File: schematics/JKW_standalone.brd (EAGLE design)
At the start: 159.4 x 80.7 mm, 225 parts, among them IC1 4093D, IC4 ATMEGA2560-16AU, Q1 BSS84, Q10 BSS84, Q11 BSS84, Q2 BSS84, Q3 BSS84, Q4 BSS84, Q5 BSS84, Q6 BSS84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

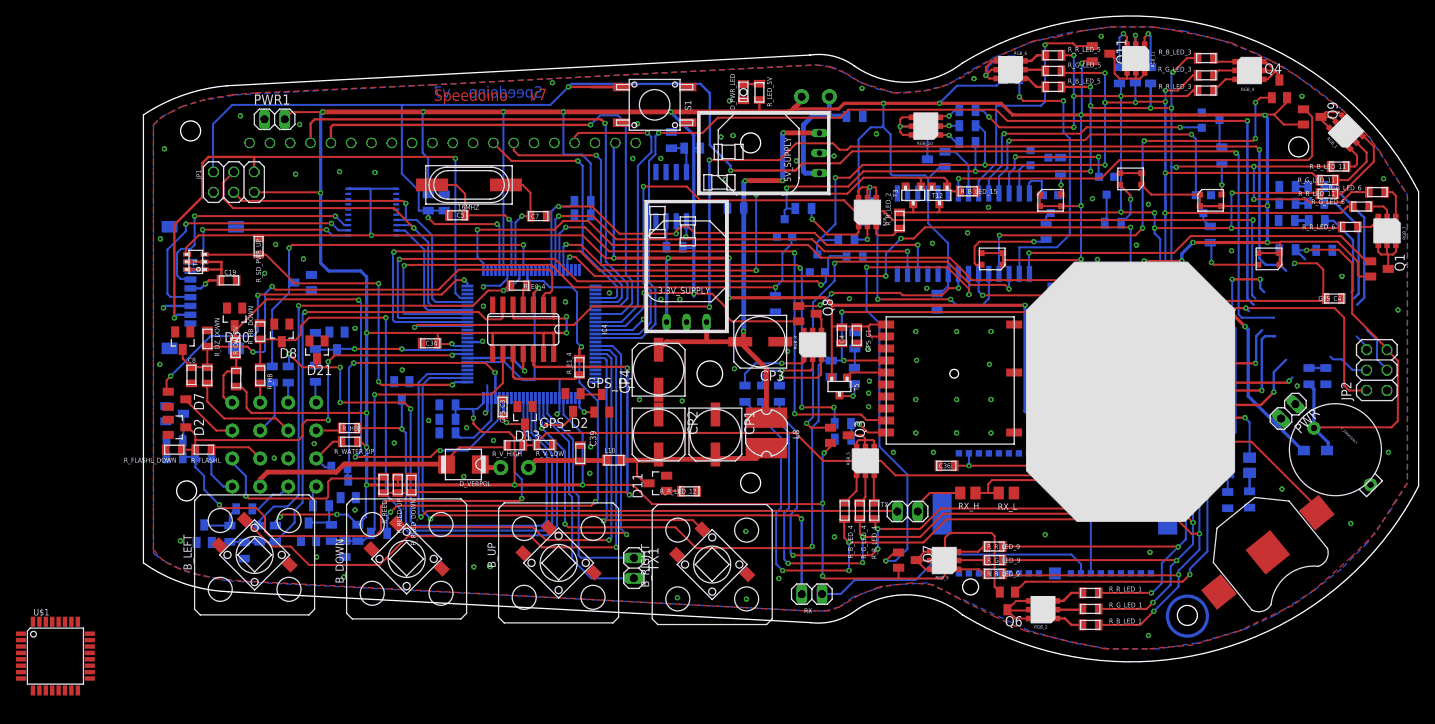
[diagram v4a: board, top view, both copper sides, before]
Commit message: Moved AT in place
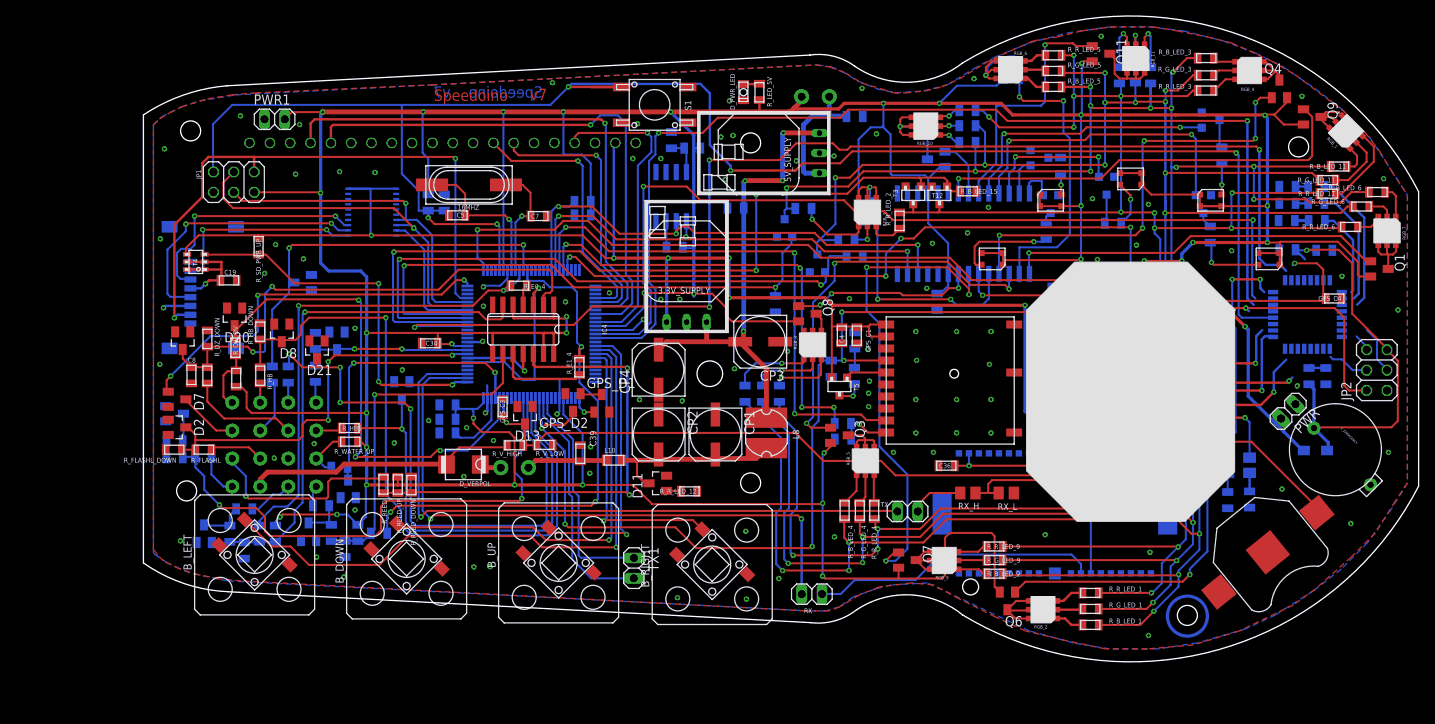
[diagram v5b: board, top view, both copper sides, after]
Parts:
- moved U$1 162.2 mm to (145.5, 38.8), flipped to the bottom, turned to 270 degrees
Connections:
- net RESETAVR_AT8: now also U$1.29
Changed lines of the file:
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@@
 <?xml version="1.0" encoding="utf-8"?>
 <!DOCTYPE eagle SYSTEM "eagle.dtd">
-<eagle version="6.2">
+<eagle version="6.1">
 <drawing>
 <settings>
@@
 <element name="U$22" library="Kolja" package="PLCC-4" value="CLM4B-RKW-CWAXBAA3" x="123.4" y="35.6" rot="R180"/>
 <element name="R_L3" library="RCLDT" package="0805" value="1k" x="125" y="43.1" rot="MR270"/>
-<element name="U$1" library="Kolja" package="TQFP8" value="ATMEGA328P-AU" x="-11" y="-3.9"/>
+<element name="U$1" library="Kolja" package="TQFP8" value="ATMEGA328P-AU" x="145.5" y="38.8" rot="MR270"/>
 </elements>
 <signals>
@@
 <wire x1="37.3017375" y1="7.03024375" x2="41.3" y2="7.25" width="0" layer="19" extent="1-1"/>
 <wire x1="119.725" y1="73.575" x2="132.2887" y2="64.0524" width="0" layer="19" extent="16-16"/>
-<wire x1="-6.7074" y1="-3.5" x2="4.625" y2="10.5" width="0" layer="19" extent="1-1"/>
-<wire x1="-15.2926" y1="-4.3" x2="-6.7074" y2="-3.5" width="0" layer="19" extent="1-1"/>
-<wire x1="-15.2926" y1="-2.7" x2="-15.2926" y2="-4.3" width="0" layer="19" extent="1-1"/>
+<wire x1="145.1" y1="34.5074" x2="4.625" y2="10.5" width="0" layer="19" extent="1-1"/>
+<wire x1="145.9" y1="43.0926" x2="145.1" y2="34.5074" width="0" layer="19" extent="1-1"/>
+<wire x1="144.3" y1="43.0926" x2="145.9" y2="43.0926" width="0" layer="19" extent="1-1"/>
 </signal>
 <signal name="DZ">
@@
 <wire x1="136.1" y1="37.5" x2="136.5" y2="37.1" width="0.254" layer="16"/>
 <contactref element="U$1" pad="32"/>
-<wire x1="-13.8" y1="0.3926" x2="118.435" y2="21.44" width="0" layer="19" extent="1-16"/>
+<wire x1="141.2074" y1="41.6" x2="118.435" y2="21.44" width="0" layer="19" extent="1-16"/>
 </signal>
 <signal name="N$9">
@@
 <wire x1="139.1" y1="59.8" x2="139.5" y2="59.4" width="0.254" layer="1"/>
 <contactref element="U$1" pad="1"/>
-<wire x1="-15.2926" y1="-1.1" x2="33.9" y2="37.2" width="0" layer="19" extent="1-16"/>
+<wire x1="142.7" y1="43.0926" x2="33.9" y2="37.2" width="0" layer="19" extent="1-16"/>
 </signal>
 <signal name="D51">
@@
 <wire x1="136.4" y1="59.2" x2="136.6" y2="59" width="0.254" layer="1"/>
 <contactref element="U$1" pad="28"/>
-<wire x1="-10.6" y1="0.3926" x2="8.76" y2="56.62" width="0" layer="19" extent="1-1"/>
+<wire x1="141.2074" y1="38.4" x2="8.76" y2="56.62" width="0" layer="19" extent="1-1"/>
 </signal>
 <signal name="N$35">
@@
 <wire x1="64" y1="58.8" x2="64" y2="61.1" width="0.254" layer="16"/>
 <contactref element="U$1" pad="30"/>
-<wire x1="-12.2" y1="0.3926" x2="56.5" y2="35.86" width="0" layer="19" extent="1-16"/>
+<wire x1="141.2074" y1="40" x2="56.5" y2="35.86" width="0" layer="19" extent="1-16"/>
 </signal>
 <signal name="RX3">
@@
 <wire x1="62.5" y1="42.7" x2="62.5" y2="54.8" width="0.254" layer="16"/>
 <contactref element="U$1" pad="31"/>
-<wire x1="-13" y1="0.3926" x2="56.5" y2="36.36" width="0" layer="19" extent="1-16"/>
+<wire x1="141.2074" y1="40.8" x2="56.5" y2="36.36" width="0" layer="19" extent="1-16"/>
 </signal>
 <signal name="NG_IN">
@@
 <wire x1="81.5" y1="24" x2="50.4" y2="24" width="0.254" layer="1"/>
 <contactref element="U$1" pad="2"/>
-<wire x1="-15.2926" y1="-1.9" x2="44.9" y2="25.8" width="0" layer="19" extent="1-1"/>
+<wire x1="143.5" y1="43.0926" x2="44.9" y2="25.8" width="0" layer="19" extent="1-1"/>
 </signal>
 <signal name="A5">
@@
 <contactref element="U$1" pad="18"/>
 <contactref element="U$1" pad="20"/>
-<wire x1="-6.7074" y1="-4.3" x2="145.7" y2="32.116" width="0" layer="19" extent="1-16"/>
-<wire x1="-6.7074" y1="-5.9" x2="-6.7074" y2="-4.3" width="0" layer="19" extent="1-1"/>
+<wire x1="145.9" y1="34.5074" x2="145.7" y2="32.116" width="0" layer="19" extent="1-16"/>
+<wire x1="147.5" y1="34.5074" x2="145.9" y2="34.5074" width="0" layer="19" extent="1-1"/>
 </signal>
 <signal name="SCK_AT8">
@@
 <wire x1="149.8" y1="33.2" x2="151.15" y2="31.85" width="0.254" layer="16"/>
 <contactref element="U$1" pad="17"/>
-<wire x1="-6.7074" y1="-6.7" x2="148.3559" y2="33.5441" width="0" layer="19" extent="1-16"/>
+<wire x1="148.3" y1="34.5074" x2="148.3559" y2="33.5441" width="0" layer="19" extent="1-16"/>
 </signal>
 <signal name="MISO_AT8">
@@
 <wire x1="152.905" y1="34.795" x2="151.6259" y2="36.0741" width="0.254" layer="16"/>
 <contactref element="U$1" pad="16"/>
-<wire x1="-8.2" y1="-8.1926" x2="151.6259" y2="36.0741" width="0" layer="19" extent="1-16"/>
+<wire x1="149.7926" y1="36" x2="151.6259" y2="36.0741" width="0" layer="19" extent="1-16"/>
 </signal>
 <signal name="MOSI_AT8">
@@
 <wire x1="155.445" y1="31.85" x2="155.445" y2="31.955" width="0.254" layer="16"/>
 <contactref element="U$1" pad="15"/>
-<wire x1="-9" y1="-8.1926" x2="152.9385" y2="36.8615" width="0" layer="19" extent="1-16"/>
+<wire x1="149.7926" y1="36.8" x2="152.9385" y2="36.8615" width="0" layer="19" extent="1-16"/>
 </signal>
 <signal name="RESETAVR_AT8">
@@
 <wire x1="125" y1="42.084" x2="123.416" y2="42.084" width="0.254" layer="16"/>
 <wire x1="123.416" y1="42.084" x2="123.4" y2="42.1" width="0.254" layer="16"/>
+<contactref element="U$1" pad="29"/>
+<wire x1="138.1889" y1="39.2111" x2="141.2074" y2="39.2" width="0" layer="19" extent="16-16"/>
 </signal>
 <signal name="P2">
@@
 <wire x1="148.7" y1="54.8" x2="147.616" y2="54.8" width="0.3048" layer="16"/>
 <contactref element="U$1" pad="11"/>
-<wire x1="-12.2" y1="-8.1926" x2="151.7111" y2="40.0111" width="0" layer="19" extent="1-16"/>
+<wire x1="149.7926" y1="40" x2="151.7111" y2="40.0111" width="0" layer="19" extent="1-16"/>
 </signal>
 <signal name="N$18">
@@
 <wire x1="149" y1="52.7" x2="147.616" y2="52.7" width="0.3048" layer="16"/>
 <contactref element="U$1" pad="10"/>
-<wire x1="-13" y1="-8.1926" x2="151.2985" y2="40.7985" width="0" layer="19" extent="1-16"/>
+<wire x1="149.7926" y1="40.8" x2="151.2985" y2="40.7985" width="0" layer="19" extent="1-16"/>
 </signal>
 <signal name="N$20">
@@
 <wire x1="147.6" y1="50.454" x2="147.686" y2="50.54" width="0.3048" layer="16"/>
 <contactref element="U$1" pad="9"/>
-<wire x1="-13.8" y1="-8.1926" x2="147.5" y2="50.5" width="0" layer="19" extent="1-16"/>
+<wire x1="149.7926" y1="41.6" x2="147.5" y2="50.5" width="0" layer="19" extent="1-16"/>
 </signal>
 <signal name="N$12">
@@
 <wire x1="142.98" y1="30.28" x2="130.43" y2="30.28" width="0.3048" layer="1"/>
 <contactref element="U$1" pad="23"/>
-<wire x1="-6.7074" y1="-1.9" x2="130.43" y2="30.28" width="0" layer="19" extent="1-1"/>
+<wire x1="143.5" y1="34.5074" x2="130.43" y2="30.28" width="0" layer="19" extent="1-1"/>
 </signal>
 <signal name="M2">
@@
 <wire x1="133.185" y1="27.52" x2="133.205" y2="27.5" width="0.3048" layer="1"/>
 <contactref element="U$1" pad="24"/>
-<wire x1="-6.7074" y1="-1.1" x2="133.185" y2="27.52" width="0" layer="19" extent="1-1"/>
+<wire x1="142.7" y1="34.5074" x2="133.185" y2="27.52" width="0" layer="19" extent="1-1"/>
 </signal>
 <signal name="M3">
@@
 <wire x1="141.2693" y1="36.0693" x2="141.3" y2="36.1" width="0.3048" layer="16"/>
 <contactref element="U$1" pad="25"/>
-<wire x1="-8.2" y1="0.3926" x2="113.615" y2="27.52" width="0" layer="19" extent="1-1"/>
+<wire x1="141.2074" y1="36" x2="113.615" y2="27.52" width="0" layer="19" extent="1-1"/>
 </signal>
 <signal name="M4">
@@
 <via x="139" y="32.7" extent="1-16" drill="0.3"/>
 <contactref element="U$1" pad="26"/>
-<wire x1="-9" y1="0.3926" x2="116.37" y2="30.28" width="0" layer="19" extent="1-1"/>
+<wire x1="141.2074" y1="36.8" x2="116.37" y2="30.28" width="0" layer="19" extent="1-1"/>
 </signal>
 <signal name="N$17">
@@
 <contactref element="U$1" pad="4"/>
 <contactref element="U$1" pad="6"/>
-<wire x1="-15.2926" y1="-3.5" x2="146.31299375" y2="24.587003125" width="0" layer="19" extent="1-1"/>
-<wire x1="-15.2926" y1="-5.1" x2="-15.2926" y2="-3.5" width="0" layer="19" extent="1-1"/>
+<wire x1="145.1" y1="43.0926" x2="146.31299375" y2="24.587003125" width="0" layer="19" extent="1-1"/>
+<wire x1="146.7" y1="43.0926" x2="145.1" y2="43.0926" width="0" layer="19" extent="1-1"/>
 </signal>
 <signal name="N$71">

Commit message: Replaced ATm8 with ATm328 in Layout
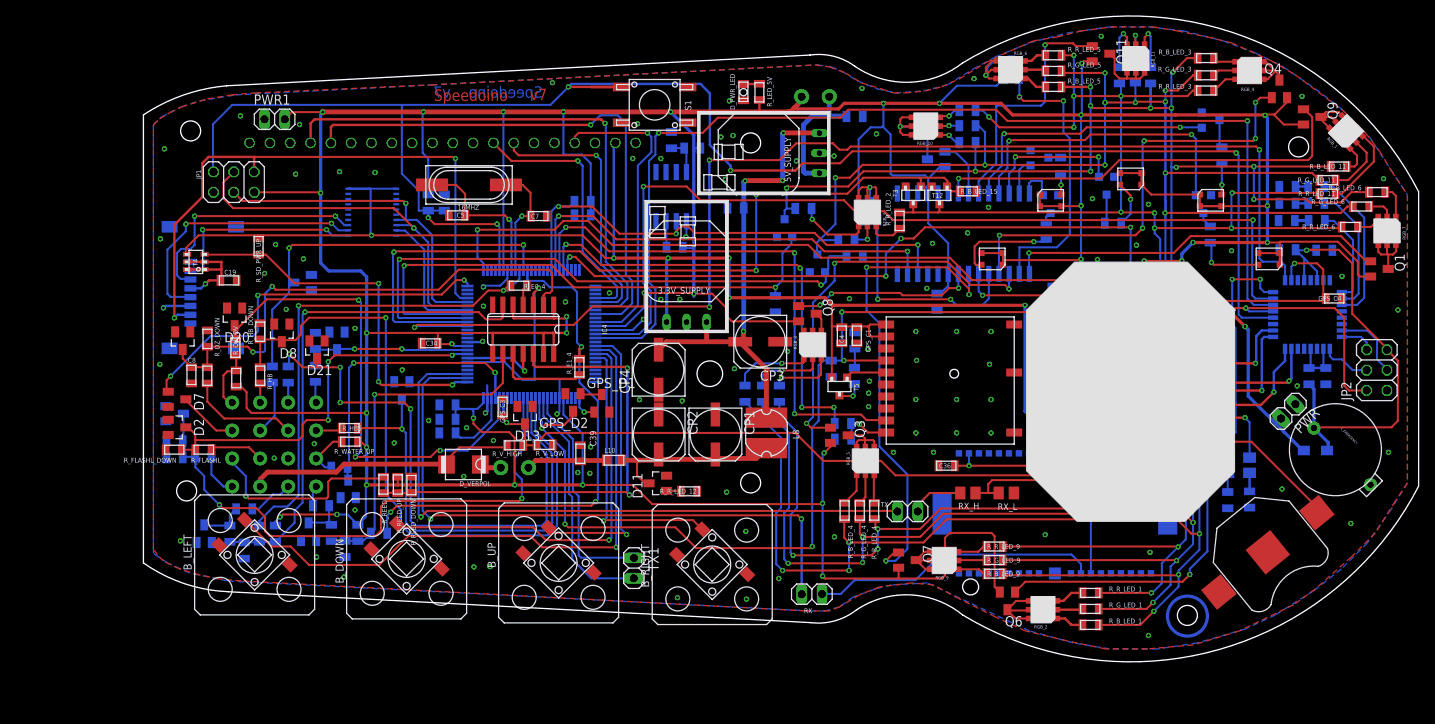
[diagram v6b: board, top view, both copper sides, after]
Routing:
- net V_AT8_BUFFERED: track 53.7 -> 59.7 mm
- net N$3: track 2.93 -> 7.50 mm
- net M1: track 13.5 -> 17.0 mm
- net MOSI_AT8: track 6.05 -> 9.17 mm
- net RESETAVR_AT8: track 128.0 -> 131.1 mm
- net TX3: track 131.7 -> 134.1 mm
- net N$14: track 17.9 -> 20.3 mm
- net A2: track 147.0 -> 149.2 mm
- net RX3: track 112.8 -> 115.0 mm
- net MISO_AT8: track 2.21 -> 4.31 mm
- net N$18: track 14.7 -> 16.2 mm
- net D6: track 150.9 -> 152.3 mm
- net M4: track 28.1 -> 29.5 mm
- net M2: track 13.5 -> 14.8 mm
- net N$20: track 11.6 -> 12.8 mm
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
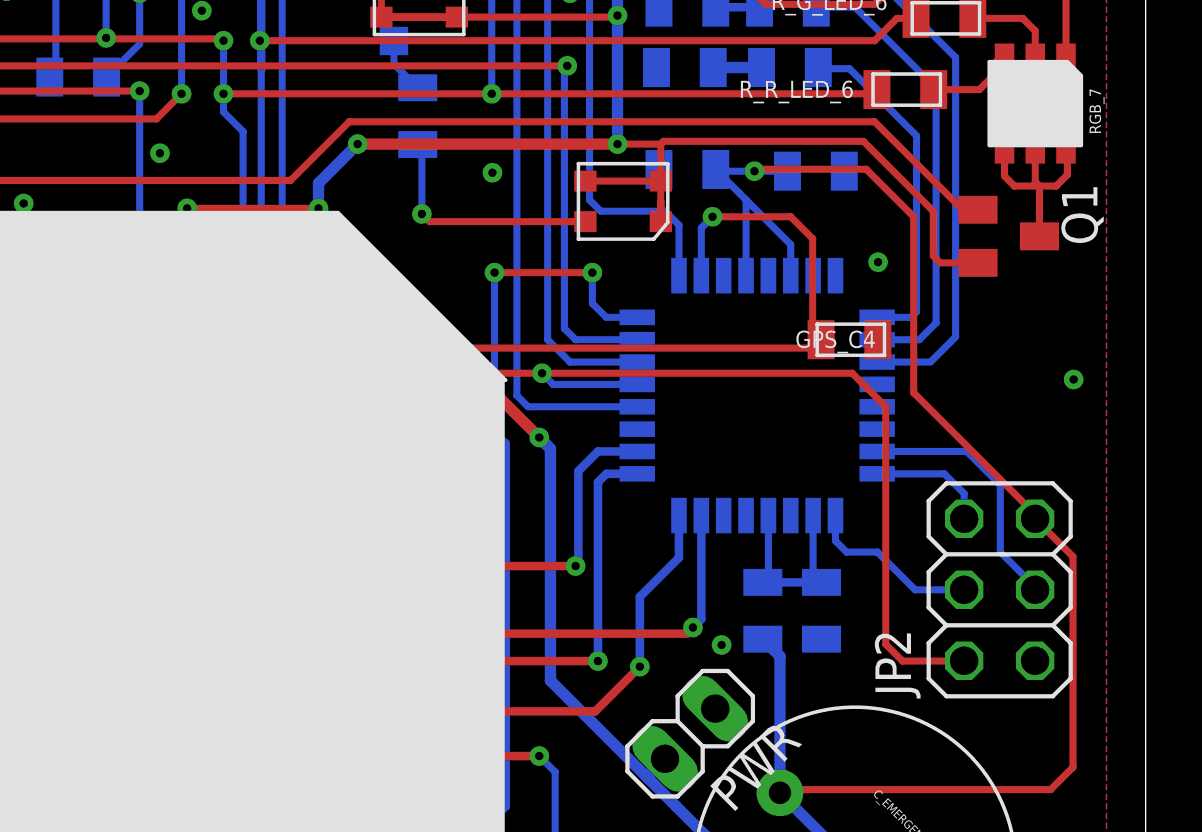
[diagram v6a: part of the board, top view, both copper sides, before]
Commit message: Added second 16Mhz crystal
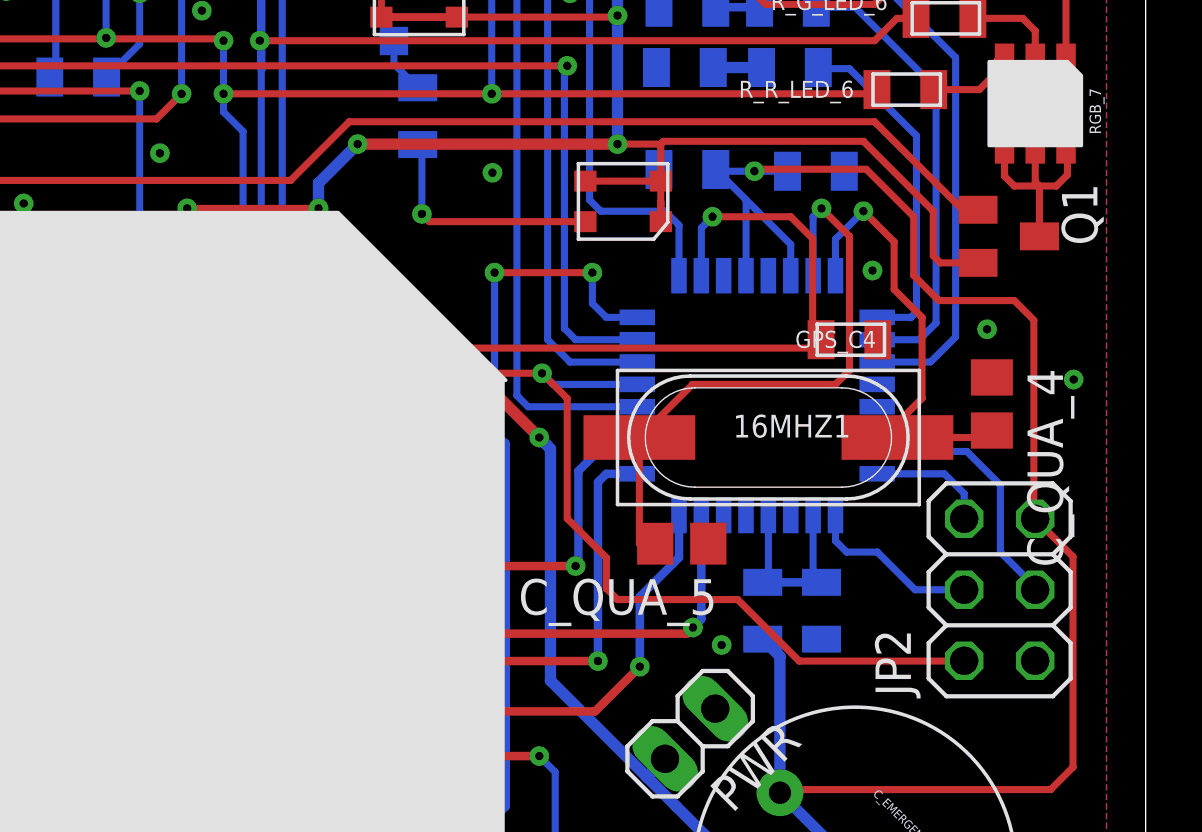
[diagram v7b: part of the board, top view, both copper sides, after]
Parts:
- added 16MHZ1: 16Mhz, XT:XT-HC49S-SMD
- added C9: 100nF, RCLDT:0805
- added C_QUA_4, C_QUA_5: 22pF, rcl:C0805
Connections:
- new net N$63: 16MHZ1.1, C_QUA_5.2, U$1.7
- new net N$65: 16MHZ1.2, C_QUA_4.2, U$1.8
- net GND: now also C9.2, C_QUA_4.1, C_QUA_5.1
- net RESETAVR_AT8: now also C9.1
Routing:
- net N$63: track 0.00 -> 21.6 mm, vias 0 -> 1
- net N$65: track 0.00 -> 15.5 mm, vias 0 -> 1
- net V_AT8_BUFFERED: track 59.7 -> 61.4 mm
- net GND: vias 105 -> 106
